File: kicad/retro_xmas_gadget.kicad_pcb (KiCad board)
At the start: 4 copper layers, 76.2 x 101.6 mm, 74 parts, among them J1 USB_C_Receptacle_USB2.0_16P, J2 SD_Card_Receptacle, J3 AudioJack3_SwitchTR, J4 Conn_01x18, J5 Conn_01x02, J6 Conn_01x03, J7 Conn_01x03, J8 Conn_01x07, Q1 UMH3N, Q2 SS8050, SW1 RESET, SW10 SELECT, SW11 START, SW12 A, SW13 B, SW2 BOOT, SW3 KH-SS12F23-G6, SW4 UP, SW5 DOWN, SW6 LEFT, SW7 RIGHT, SW8 MENU, SW9 OPTION, U1 CP2102N-Axx-xQFN28, U2 ESP32-S3-WROOM-1, U4 XC6210B332MR, U5 TP4056

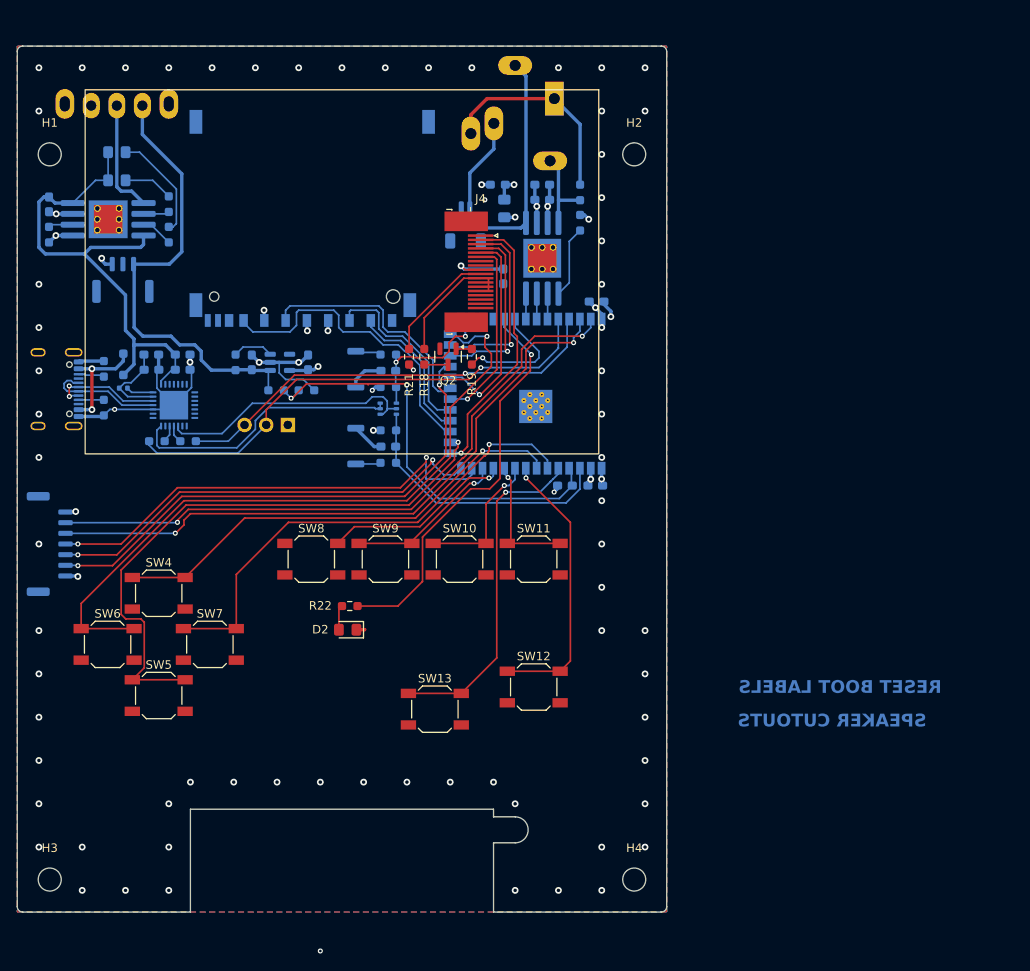
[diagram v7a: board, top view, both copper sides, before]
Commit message: adjustments with 3d model
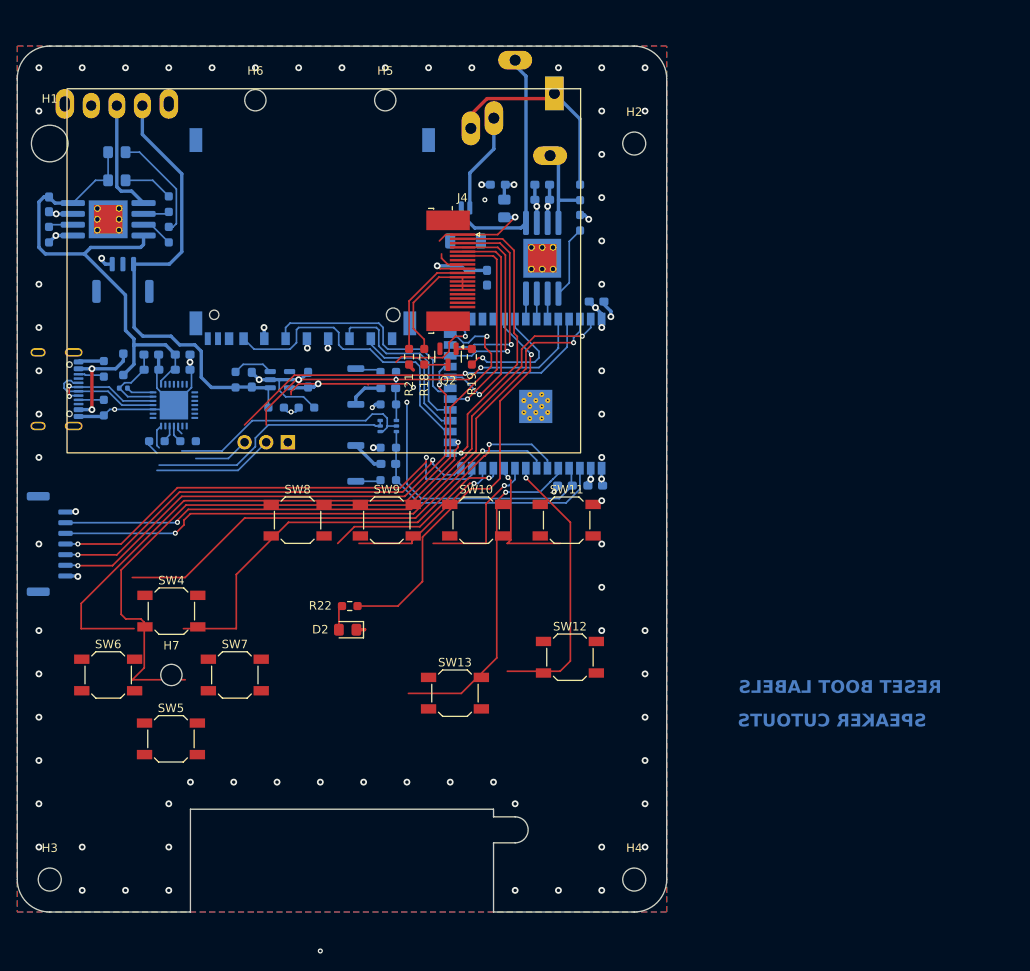
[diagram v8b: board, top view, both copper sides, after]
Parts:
- added H5: MountingHole, MountingHole:MountingHole_2.5mm, F.Cu at (68.6, 57.1)
- added H6: MountingHole, MountingHole:MountingHole_2.5mm, F.Cu at (53.3, 57.1)
- added H7: MountingHole, MountingHole:MountingHole_2.5mm, F.Cu at (43.5, 124.6)
- H1: footprint MountingHole:MountingHole_2.7mm_M2.5 -> MountingHole:MountingHole_4.3mm_M4
- moved SW11 5.99 mm to (89.9, 106.4)
- moved SW12 5.50 mm to (90.2, 122.5)
- moved SW5 5.28 mm to (43.4, 132.1)
- moved SW10 4.97 mm to (79.2, 106.4)
- moved SW8 4.85 mm to (58.3, 106.4)
- moved SW7 4.63 mm to (50.9, 124.6)
- moved SW9 4.58 mm to (68.8, 106.4)
- moved SW6 3.59 mm to (36.1, 124.6)
- moved SW13 3.02 mm to (76.8, 126.7)
- moved SW4 2.57 mm to (43.5, 117.1)
- moved J2 2.14 mm to (60.0, 73.2)
- moved J4 2.13 mm to (77.2, 77.2)
- moved R5 2.03 mm to (68.9, 101.7)
- moved SW1 2.03 mm to (65.1, 99.8)
- moved C12 2.03 mm to (52.9, 89.9)
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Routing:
- net GND: track 76.2 -> 89.5 mm
- net /TFT_RST: track 32.4 -> 34.6 mm
- net /TFT_SDI: track 21.8 -> 24.0 mm
- net /TFT_SCL: track 22.0 -> 24.2 mm
- net /TFT_DC: track 21.6 -> 23.8 mm
- net /TFT_CS: track 24.1 -> 26.3 mm
- net /VBAT_ON: track 53.9 -> 55.9 mm
- net VCC: track 21.8 -> 23.3 mm
- net /VBAT_SENSE: track 50.5 -> 49.3 mm
- net /SD_CD: track 17.3 -> 16.4 mm
- net /SD_DAT: track 36.4 -> 35.5 mm
- net /EN: track 32.4 -> 31.5 mm
- net /TFT_LEDK: track 13.7 -> 14.5 mm
- net /SD_CLK: track 28.0 -> 27.2 mm
- net /SD_CMD: track 21.6 -> 20.8 mm
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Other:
- outline, holes or cut-outs redrawn
